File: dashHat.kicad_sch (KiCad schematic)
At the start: 18 parts, among them J1 Input, J2 LCD, J3 GPIO, J4 LEDs, Q1 BSS138, Q2 BSS138, U1 CAT24C256

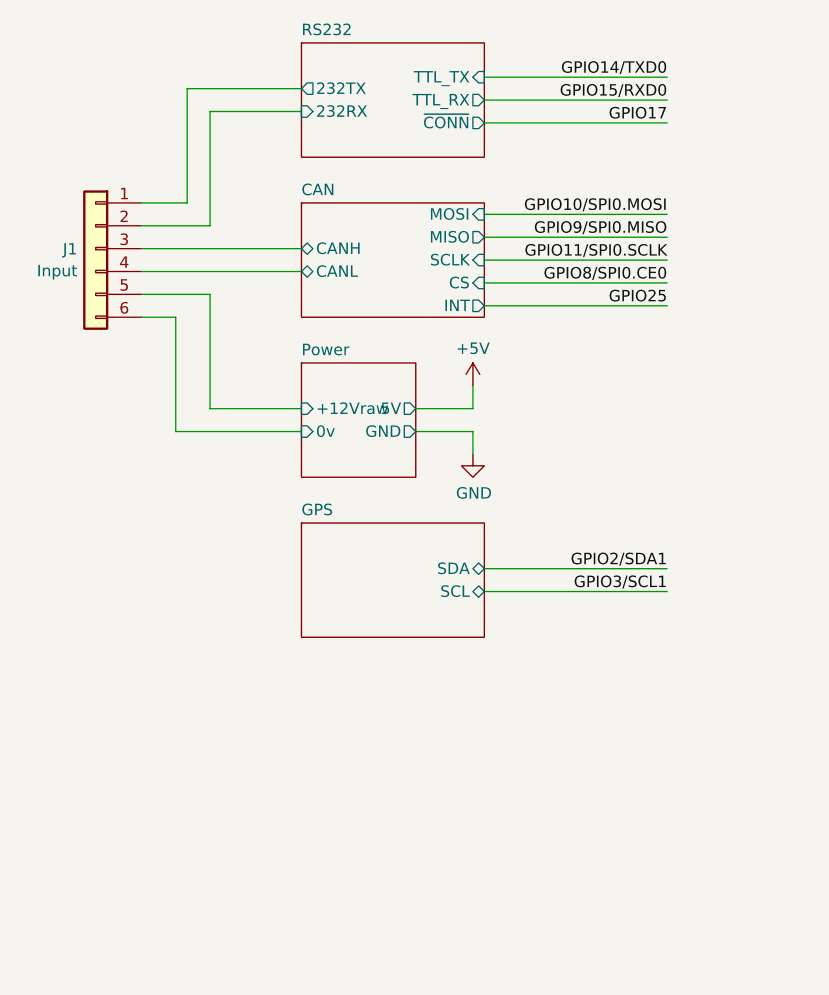
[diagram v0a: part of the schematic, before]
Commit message: added 4 inputs and 2 pwm outputs, completed routing
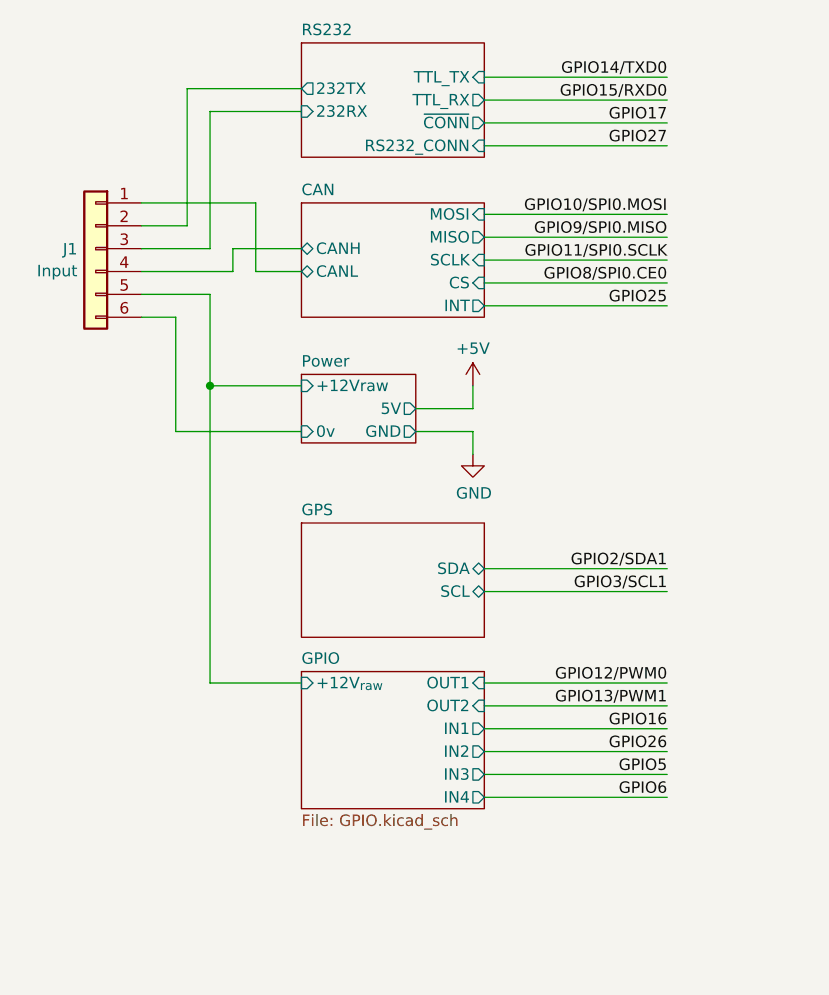
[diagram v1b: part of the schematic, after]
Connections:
- net CAN/CANH: now also J1.4 (Pin_4); no longer J1.3 (Pin_3)
- net CAN/CANL: now also J1.1 (Pin_1); no longer J1.4 (Pin_4)
- net RS232/232RX: now also J1.3 (Pin_3); no longer J1.2 (Pin_2)
- net RS232/232TX: now also J1.2 (Pin_2); no longer J1.1 (Pin_1)
- net Power/+12Vraw renamed GPIO/+12V_{raw}
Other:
- added sheet GPIO (GPIO.kicad_sch)
- sheet RS232 ports: added RS232_CONN; removed none

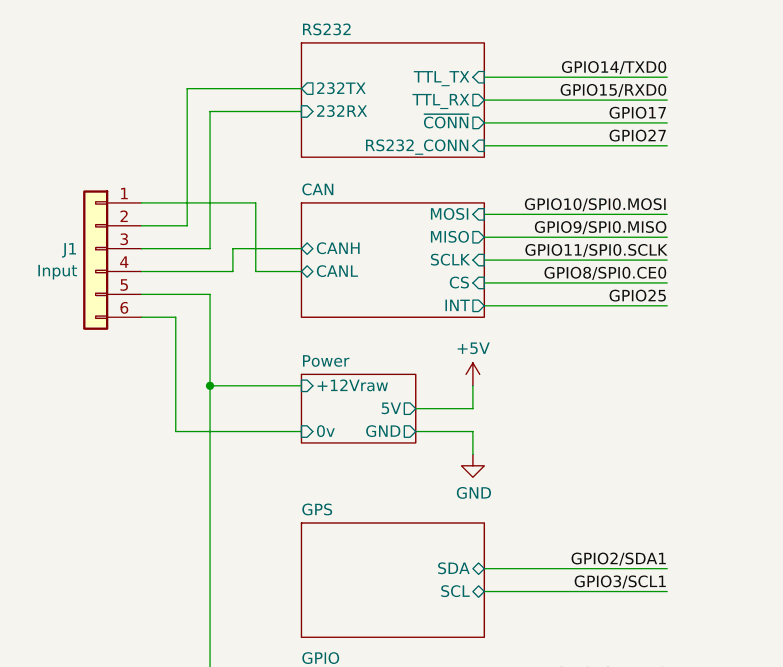
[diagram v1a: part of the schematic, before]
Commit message: revised schematic after initial layout  - all connectors are vertical  - increased current handling of outputs  - replaced mechanical relay with ssr  - jumper to disable gps antenna power
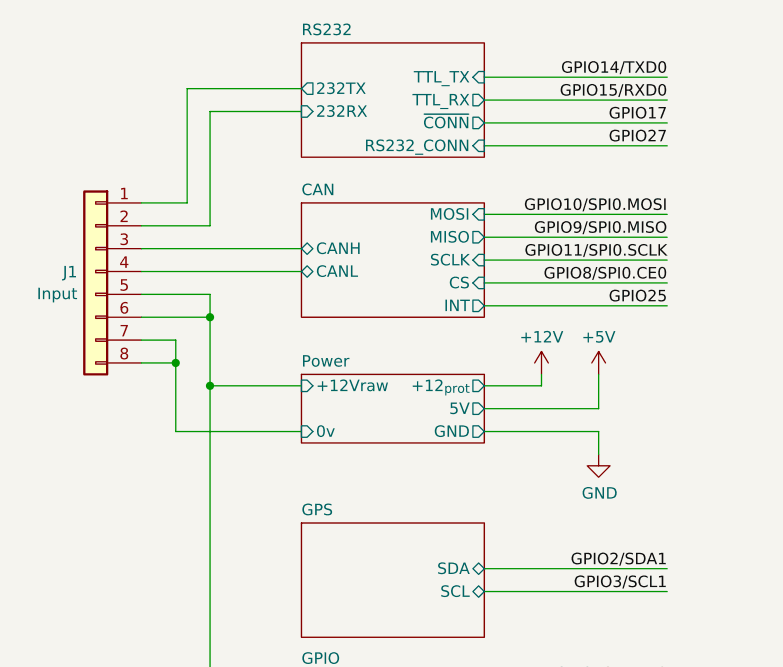
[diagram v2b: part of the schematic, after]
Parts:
- C1: footprint Capacitor_SMD:C_0603_1608Metric_Pad1.08x0.95mm_HandSolder -> Capacitor_SMD:C_0603_1608Metric
- D1: footprint LED_SMD:LED_0603_1608Metric_Pad1.05x0.95mm_HandSolder -> LED_SMD:LED_0603_1608Metric
- F1: footprint Fuse:Fuse_1812_4532Metric_Pad1.30x3.40mm_HandSolder -> Fuse:Fuse_1812_4532Metric
- J1: footprint Connector_Molex:Molex_Nano-Fit_105314-xx06_2x03_P2.50mm_Horizontal -> Connector_Molex:Molex_Nano-Fit_105310-xx08_2x04_P2.50mm_Vertical; symbol Connector_Generic:Conn_01x06 -> Connector_Generic:Conn_01x08; Mfg Part Number 105314-1106 -> 105310-1108
- J4: footprint Connector_Molex:Molex_Nano-Fit_105314-xx04_2x02_P2.50mm_Horizontal -> Connector_JST:JST_PH_B4B-PH-K_1x04_P2.00mm_Vertical
- R1, R2, R3, R4, R5, R6, R7: footprint Resistor_SMD:R_0603_1608Metric_Pad0.98x0.95mm_HandSolder -> Resistor_SMD:R_0603_1608Metric
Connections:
- net CAN/CANH: now also J1.3 (Pin_3); no longer J1.4 (Pin_4)
- net CAN/CANL: now also J1.4 (Pin_4); no longer J1.1 (Pin_1)
- net GPIO/+12V_{raw}: now also J1.6 (Pin_6)
- net Power/0v: now also J1.7 (Pin_7), J1.8 (Pin_8); no longer J1.6 (Pin_6)
- net RS232/232RX: now also J1.2 (Pin_2); no longer J1.3 (Pin_3)
- net RS232/232TX: now also J1.1 (Pin_1); no longer J1.2 (Pin_2)
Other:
- sheet Power ports: added +12_{prot}; removed none

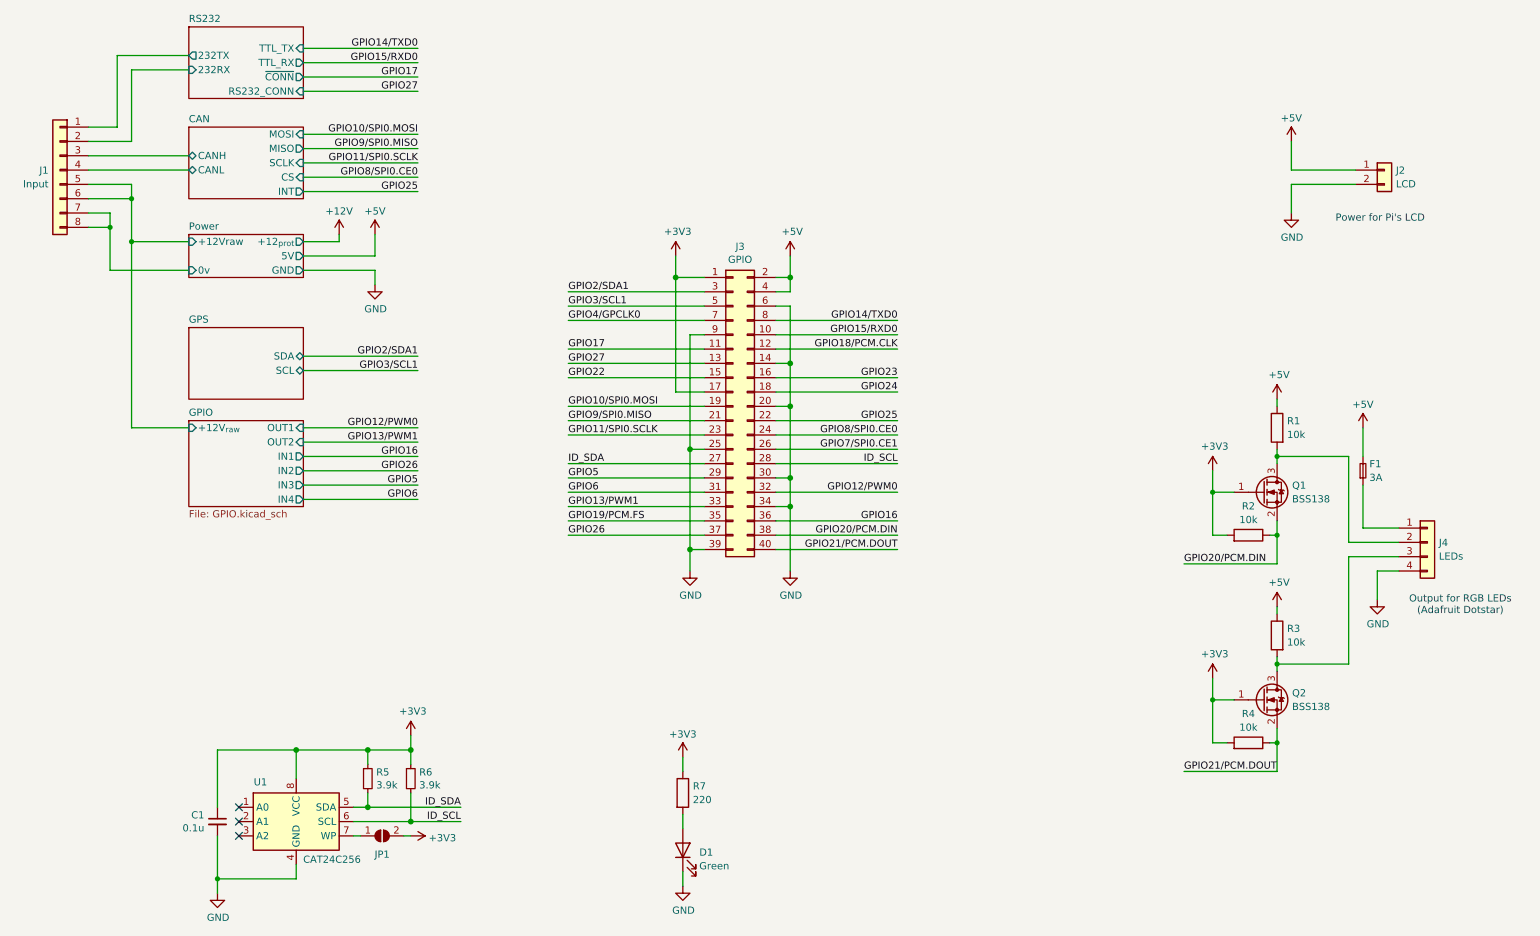
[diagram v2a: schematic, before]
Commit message: second pass at layout complete
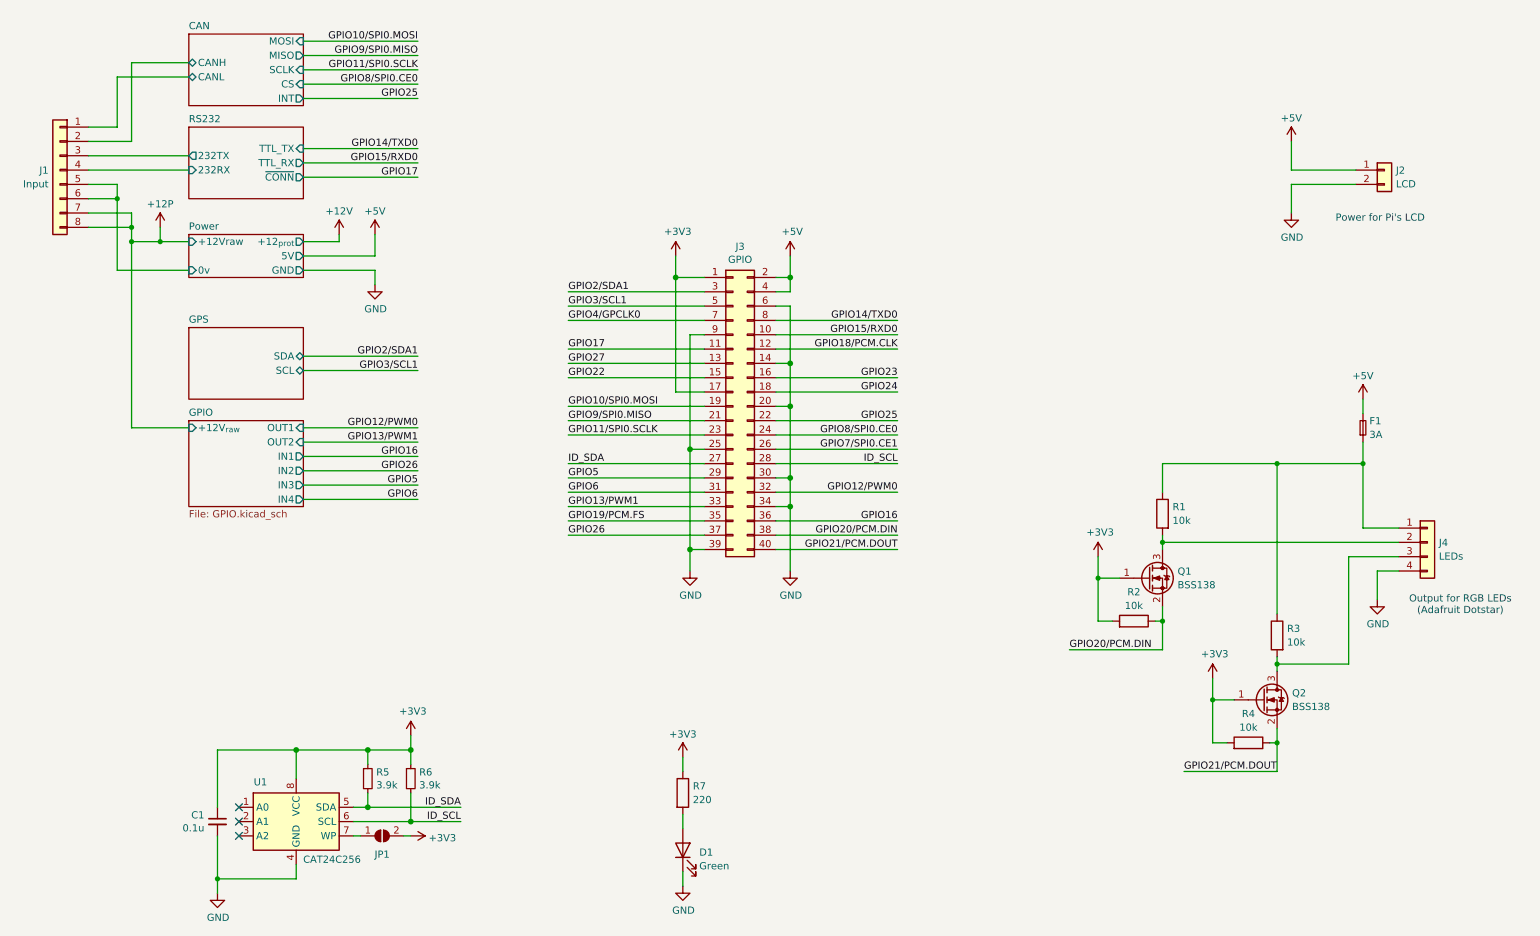
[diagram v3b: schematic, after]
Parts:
- J4: footprint Connector_JST:JST_PH_B4B-PH-K_1x04_P2.00mm_Vertical -> Connector_Molex:Molex_Nano-Fit_105310-xx04_2x02_P2.50mm_Vertical
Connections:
- net GPIO/+12V_{raw} is gone; now on net Power/0v: J1.5 (Pin_5), J1.6 (Pin_6)
- net +5V: no longer R1.1, R3.1
- net CAN/CANH: now also J1.2 (Pin_2); no longer J1.3 (Pin_3)
- net CAN/CANL: now also J1.1 (Pin_1); no longer J1.4 (Pin_4)
- net Power/0v: no longer J1.7 (Pin_7), J1.8 (Pin_8)
- net RS232/232RX: now also J1.4 (Pin_4); no longer J1.2 (Pin_2)
- net RS232/232TX: now also J1.3 (Pin_3); no longer J1.1 (Pin_1)
- net at F1.1, J4.1 (Pin_1): now also R1.1, R3.1
- new net +12P: J1.7 (Pin_7), J1.8 (Pin_8)
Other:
- sheet RS232 ports: added none; removed RS232_CONN
- moved on the sheet: F1, Q1, R1, R2

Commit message: add a version, add uart test pads to gps, sent for manufacturing
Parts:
- Q1, Q2: value BSS138 -> 2N7002
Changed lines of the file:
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@@
 			)
 		)
-		(property "Value" "BSS138"
+		(property "Value" "2N7002"
 			(at 243.967 144.7221 0)
 			(effects
@@
 			)
 		)
-		(property "Datasheet" "https://www.onsemi.com/pub/Collateral/BSS138-D.PDF"
+		(property "Datasheet" "https://www.onsemi.com/pub/Collateral/NDS7002A-D.PDF"
 			(at 243.84 147.32 0)
 			(effects
@@
 			)
 		)
-		(property "Value" "BSS138"
+		(property "Value" "2N7002"
 			(at 223.647 123.1321 0)
 			(effects
@@
 			)
 		)
-		(property "Datasheet" "https://www.onsemi.com/pub/Collateral/BSS138-D.PDF"
+		(property "Datasheet" "https://www.onsemi.com/pub/Collateral/NDS7002A-D.PDF"
 			(at 223.52 125.73 0)
 			(effects

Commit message: filled in mfg part number for ordering
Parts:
- J2: Mfg Part Number (none) -> --
- J4: Mfg Part Number 105314-1104 -> 105310-1104
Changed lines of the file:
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@@
 			)
 		)
-		(property "Mfg Part Number" "105314-1104"
+		(property "Mfg Part Number" "105310-1104"
 			(at 267.97 115.57 0)
 			(effects
@@
 			(at 260.35 49.53 0)
 			(effects
+				(font
+					(size 1.27 1.27)
+				)
+				(hide yes)
+			)
+		)
+		(property "Mfg Part Number" "--"
+			(at 260.35 49.53 0)
+			(effects

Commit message: bug fixes from testing
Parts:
- Q1, Q2: value 2N7002 -> BSS138
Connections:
- net +3V3: now also U1.2 (A1)
- net +12P renamed Power/+12v_raw
- no-connect marks 3 -> 2
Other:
- sheet Power ports: added +12v_raw; removed +12Vraw
- note added: "Addr: 0x52"
- moved on the sheet: C1
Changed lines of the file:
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@@
 	)
 	(junction
-		(at 53.34 175.26)
+		(at 46.99 175.26)
 		(diameter 0)
 		(color 0 0 0 0)
@@
 	)
 	(junction
-		(at 38.1 62.23)
-		(diameter 0)
+		(at 154.94 109.22)
+		(diameter 1.016)
 		(color 0 0 0 0)
 	)
 	(junction
-		(at 154.94 109.22)
-		(diameter 1.016)
+		(at 52.07 152.4)
+		(diameter 0)
 		(color 0 0 0 0)
 	)
@@
 	)
 	(junction
-		(at 43.18 62.23)
-		(diameter 0)
-		(color 0 0 0 0)
-	)
-	(junction
 		(at 35.56 54.61)
 		(diameter 0)
@@
 	)
 	(no_connect
-		(at 57.15 165.1)
-	)
-	(no_connect
 		(at 57.15 167.64)
 	)
@@
 	(wire
 		(pts
-			(xy 38.1 59.69) (xy 38.1 62.23)
-		)
-		(stroke
-			(width 0)
-			(type default)
-		)
-	)
-	(wire
-		(pts
 			(xy 139.7 101.6) (xy 115.57 101.6)
 		)
@@
 	(wire
 		(pts
+			(xy 52.07 165.1) (xy 52.07 152.4)
+		)
+		(stroke
+			(width 0)
+			(type default)
+		)
+	)
+	(wire
+		(pts
 			(xy 38.1 30.48) (xy 38.1 44.45)
 		)
@@
 	(wire
 		(pts
+			(xy 48.26 63.5) (xy 38.1 63.5)
+		)
+		(stroke
+			(width 0)
+			(type default)
+		)
+	)
+	(wire
+		(pts
 			(xy 115.57 83.82) (xy 139.7 83.82)
 		)
@@
 	(wire
 		(pts
-			(xy 152.4 81.28) (xy 173.99 81.28)
+			(xy 57.15 165.1) (xy 52.07 165.1)
 		)
 		(stroke
 			(width 0)
-			(type solid)
+			(type default)
 		)
 	)
 	(wire
 		(pts
-			(xy 43.18 62.23) (xy 48.26 62.23)
+			(xy 152.4 81.28) (xy 173.99 81.28)
 		)
 		(stroke
 			(width 0)
-			(type default)
+			(type solid)
 		)
 	)
@@
 	(wire
 		(pts
-			(xy 224.79 156.21) (xy 241.3 156.21)
+			(xy 38.1 59.69) (xy 38.1 63.5)
 		)
 		(stroke
@@
 	(wire
 		(pts
-			(xy 154.94 73.66) (xy 152.4 73.66)
+			(xy 224.79 156.21) (xy 241.3 156.21)
 		)
 		(stroke
 			(width 0)
-			(type solid)
+			(type default)
 		)
 	)
 	(wire
 		(pts
-			(xy 68.58 85.09) (xy 88.9 85.09)
+			(xy 154.94 73.66) (xy 152.4 73.66)
 		)
 		(stroke
 			(width 0)
-			(type default)
+			(type solid)
 		)
 	)
 	(wire
 		(pts
-			(xy 48.26 95.25) (xy 38.1 95.25)
+			(xy 68.58 85.09) (xy 88.9 85.09)
 		)
 		(stroke
@@
 	(wire
 		(pts
-			(xy 38.1 62.23) (xy 43.18 62.23)
+			(xy 46.99 152.4) (xy 46.99 162.56)
 		)
 		(stroke
 			(width 0)
-			(type default)
+			(type solid)
 		)
 	)
 	(wire
 		(pts
-			(xy 53.34 152.4) (xy 53.34 162.56)
+			(xy 46.99 167.64) (xy 46.99 175.26)
 		)
 		(stroke
@@
 	(wire
 		(pts
-			(xy 53.34 167.64) (xy 53.34 175.26)
+			(xy 46.99 175.26) (xy 67.31 175.26)
 		)
 		(stroke
@@
 	(wire
 		(pts
-			(xy 53.34 175.26) (xy 67.31 175.26)
+			(xy 67.31 152.4) (xy 52.07 152.4)
 		)
 		(stroke
@@
 	(wire
 		(pts
-			(xy 67.31 152.4) (xy 53.34 152.4)
+			(xy 52.07 152.4) (xy 46.99 152.4)
 		)
 		(stroke
@@
 	(wire
 		(pts
-			(xy 53.34 175.26) (xy 53.34 177.8)
+			(xy 46.99 175.26) (xy 46.99 177.8)
 		)
 		(stroke
@@
 	(wire
 		(pts
-			(xy 38.1 95.25) (xy 38.1 62.23)
-		)
-		(stroke
-			(width 0)
-			(type default)
-		)
-	)
-	(wire
-		(pts
 			(xy 259.08 125.73) (xy 259.08 120.65)
 		)
@@
 	(wire
 		(pts
-			(xy 43.18 59.69) (xy 43.18 62.23)
-		)
-		(stroke
-			(width 0)
-			(type default)
-		)
-	)
-	(wire
-		(pts
 			(xy 35.56 52.07) (xy 35.56 54.61)
 		)
@@
 		)
 	)
+	(text "Addr: 0x52"
+		(exclude_from_sim no)
+		(at 58.674 172.72 0)
+		(effects
+			(font
+				(size 1.27 1.27)
+			)
+		)
+	)
 	(text "Power for Pi's LCD"
 		(exclude_from_sim no)
@@
 	(symbol
 		(lib_id "Device:C_Small")
-		(at 53.34 165.1 0)
+		(at 46.99 165.1 0)
 		(unit 1)
 		(exclude_from_sim no)
@@
 		(dnp no)
 		(property "Reference" "C1"
-			(at 51.0158 163.9506 0)
+			(at 44.6658 163.9506 0)
 			(effects
 				(font
@@
 		)
 		(property "Value" "0.1u"
-			(at 51.0158 166.2493 0)
+			(at 44.6658 166.2493 0)
 			(effects
 				(font
@@
 		)
 		(property "Footprint" "Capacitor_SMD:C_0603_1608Metric"
-			(at 53.34 165.1 0)
+			(at 46.99 165.1 0)
 			(effects
 				(font
@@
 		)
 		(property "Datasheet" "~"
-			(at 53.34 165.1 0)
+			(at 46.99 165.1 0)
 			(effects
 				(font
@@
 		)
 		(property "Description" ""
-			(at 53.34 165.1 0)
+			(at 46.99 165.1 0)
 			(effects
 				(font
@@
 		)
 		(property "Mfg Part Number" "CGA3E2X8R1E104K080AA"
-			(at 53.34 165.1 0)
+			(at 46.99 165.1 0)
 			(effects
 				(font
@@
 			)
 		)
-		(property "Value" "2N7002"
+		(property "Value" "BSS138"
 			(at 243.967 144.7221 0)
 			(effects
@@
 	(symbol
 		(lib_id "power:GND")
-		(at 53.34 177.8 0)
+		(at 46.99 177.8 0)
 		(unit 1)
 		(exclude_from_sim no)
@@
 		(dnp no)
 		(property "Reference" "#PWR019"
-			(at 53.34 184.15 0)
+			(at 46.99 184.15 0)
 			(effects
 				(font
@@
 		)
 		(property "Value" "GND"
-			(at 53.4543 182.1244 0)
+			(at 47.1043 182.1244 0)
 			(effects
 				(font
@@
 		)
 		(property "Footprint" ""
-			(at 53.34 177.8 0)
+			(at 46.99 177.8 0)
 			(effects
 				(font
@@
 		)
 		(property "Datasheet" ""
-			(at 53.34 177.8 0)
+			(at 46.99 177.8 0)
 			(effects
 				(font
@@
 		)
 		(property "Description" ""
-			(at 53.34 177.8 0)
+			(at 46.99 177.8 0)
 			(effects
 				(font
@@
 	)
 	(symbol
-		(lib_id "power:+12P")
-		(at 43.18 59.69 0)
-		(unit 1)
-		(exclude_from_sim no)
-		(in_bom yes)
-		(on_board yes)
-		(dnp no)
-		(fields_autoplaced yes)
-		(property "Reference" "#PWR058"
-			(at 43.18 63.5 0)
-			(effects
-				(font
-					(size 1.27 1.27)
-				)
-				(hide yes)
-			)
-		)
-		(property "Value" "+12P"
-			(at 43.18 55.5569 0)
-			(effects
-				(font
-					(size 1.27 1.27)
-				)
-			)
-		)
-		(property "Footprint" ""
-			(at 43.18 59.69 0)
-			(effects
-				(font
-					(size 1.27 1.27)
-				)
-				(hide yes)
-			)
-		)
-		(property "Datasheet" ""
-			(at 43.18 59.69 0)
-			(effects
-				(font
-					(size 1.27 1.27)
-				)
-				(hide yes)
-			)
-		)
-		(property "Description" "Power symbol creates a global label with name \"+12P\""
-			(at 43.18 59.69 0)
-			(effects
-				(font
-					(size 1.27 1.27)
-				)
-				(hide yes)
-			)
-		)
-		(pin "1"
-		)
-		(instances
-			(project "dashHat"
-				(path "/e63e39d7-6ac0-4ffd-8aa3-1841a4541b55"
-					(reference "#PWR058")
-					(unit 1)
-				)
-			)
-		)
-	)
-	(symbol
 		(lib_name "+5V_2")
 		(lib_id "power:+5V")
@@
 			)
 		)
-		(property "Value" "2N7002"
+		(property "Value" "BSS138"
 			(at 223.647 123.1321 0)
 			(effects
@@
 			)
 		)
-		(pin "+12Vraw" input
-			(at 48.26 62.23 180)
+		(pin "+12_{prot}" output
+			(at 68.58 62.23 0)
 			(effects
 				(font
 					(size 1.27 1.27)
 				)
-				(justify left)
+				(justify right)
 			)
 		)
-		(pin "+12_{prot}" output
-			(at 68.58 62.23 0)
+		(pin "+12v_raw" input
+			(at 48.26 63.5 180)
 			(effects
 				(font
 					(size 1.27 1.27)
 				)
-				(justify right)
+				(justify left)
 			)
 		)
